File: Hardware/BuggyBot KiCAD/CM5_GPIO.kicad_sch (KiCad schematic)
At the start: 25 parts, among them J14 JST_SHBM04B-SRSS-TB, J2 Conn_02x07_Odd_Even, J3 Conn_01x03, J8 THD-20-R, J9 THD-02-R, SW1 Right angle Tact button, U1 TPD4EUSB30, U2 TPD4EUSB30, U3 MagJack-A70-112-331N126

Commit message: Removed all unnecessary components and modified PCB
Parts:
- removed J3: Conn_01x03, Connector_PinHeader_2.54mm:PinHeader_1x03_P2.54mm_Vertical, symbol Connector_Generic:Conn_01x03
- removed J9: THD-02-R, Connector_PinHeader_2.54mm:PinHeader_2x02_P2.54mm_Vertical, symbol Connector_Generic:Conn_02x02_Odd_Even
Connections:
- net BT_nDis: no longer names the net of Module1.91 (BT_nDisable)
- net SD_CLK: no longer names the net of Module1.57 (SD_CLK)
- net SD_CMD: no longer names the net of Module1.62 (SD_CMD)
- net SD_DAT0: no longer names the net of Module1.63 (SD_DAT0)
- net SD_DAT1: no longer names the net of Module1.67 (SD_DAT1)
- net SD_DAT2: no longer names the net of Module1.69 (SD_DAT2)
- net SD_DAT3: no longer names the net of Module1.61 (SD_DAT3)
- net SD_PWR_ON: no longer names the net of Module1.75 (SD_PWR_ON)
- net TR0_TAP: no longer names the net of U3.11 (VC1)
- net TR1_TAP: no longer names the net of U3.12 (VC2)
- net TR2_TAP: no longer names the net of U3.13 (VC3)
- net TR3_TAP: no longer names the net of U3.14 (VC4)
- net WL_nDis: no longer names the net of Module1.89 (WiFi_nDisable)
- no-connect marks 6 -> 19
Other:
- note added: "Activity LED (KEEP)"
- note added: "J3 removed and No-connect flags added. 10/12/26"
- note added: "POE Header removed and No-connect flags added to ethernet 10/12/26"
- note added: "PWR LED (KEEP)"
- note removed: "Activity LED"
- note removed: "Not Fitted header"
- note removed: "POE Header"
- note removed: "PWR LED"

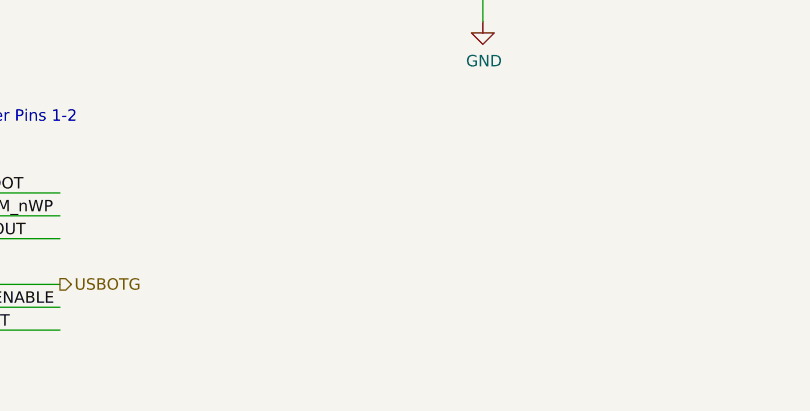
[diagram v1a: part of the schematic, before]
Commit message: Added quick connect port for IMU
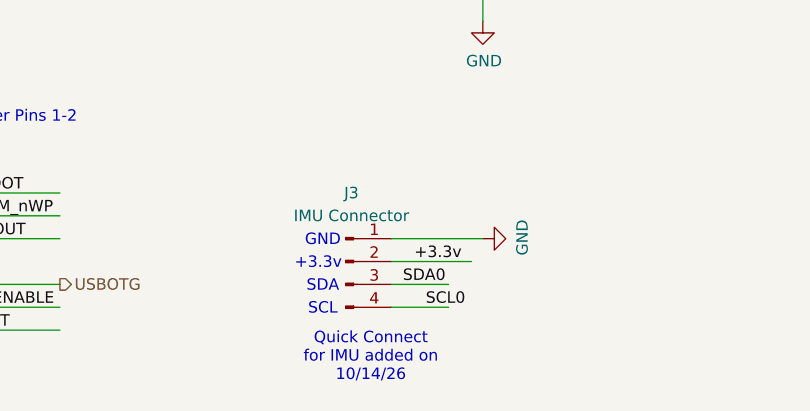
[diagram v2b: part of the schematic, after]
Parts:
- added J3: IMU Connector, Connector_JST:JST_SH_SM04B-SRSS-TB_1x04-1MP_P1.00mm_Horizontal, symbol Connector:Conn_01x04_Pin
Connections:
- net +3.3v: now also J3.2 (Pin_2)
- net GND: now also J3.1 (Pin_1)
- net SCL0: now also J3.4 (Pin_4)
- net SDA0: now also J3.3 (Pin_3)
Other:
- note added: "+3.3v"
- note added: "GND"
- note added: "Quick Connect for IMU added on 10/14/26"
- note added: "SCL"
- note added: "SDA"

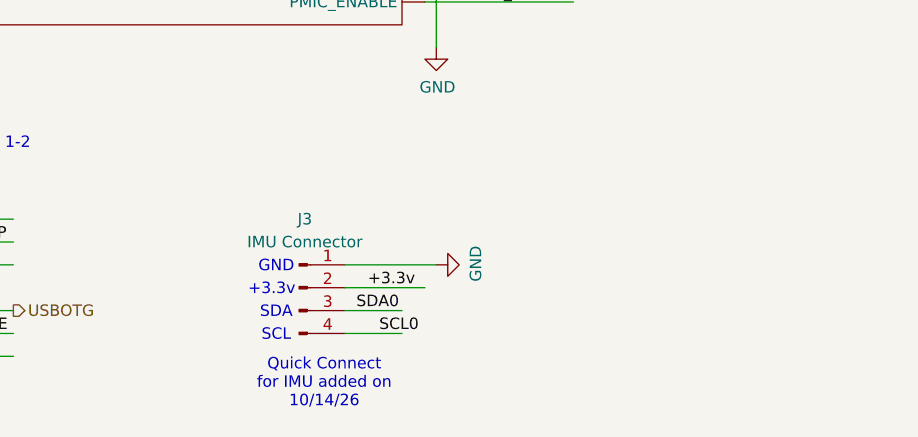
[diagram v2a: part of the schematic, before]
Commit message: Added connection port for LCD
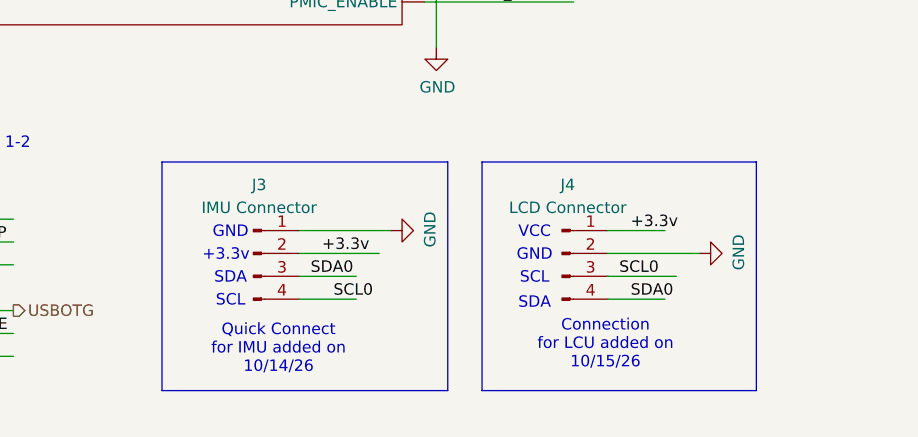
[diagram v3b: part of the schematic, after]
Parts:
- added J4: LCD Connector, Connector_JST:JST_PH_S4B-PH-K_1x04_P2.00mm_Horizontal, symbol Connector:Conn_01x04_Pin
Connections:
- net +3.3v: now also J4.1 (Pin_1)
- net GND: now also J4.2 (Pin_2)
- net SCL0: now also J4.3 (Pin_3)
- net SDA0: now also J4.4 (Pin_4)
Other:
- note added: "Connection for LCU added on 10/15/26"
- note added: "VCC"
- moved on the sheet: J3

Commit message: Updated KiCad files
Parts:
- J4: footprint Connector_JST:JST_PH_S4B-PH-K_1x04_P2.00mm_Horizontal -> Connector_JST:JST_SH_SM04B-SRSS-TB_1x04-1MP_P1.00mm_Horizontal
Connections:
- net +3.3v: now also J4.2 (Pin_2); no longer J4.1 (Pin_1)
- net GND: now also J4.1 (Pin_1); no longer J4.2 (Pin_2)
- net SCL0: now also J4.4 (Pin_4); no longer J4.3 (Pin_3)
- net SDA0: now also J4.3 (Pin_3); no longer J4.4 (Pin_4)
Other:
- note added: "Connection for LCU modified on 10/22/26"
- note removed: "Connection for LCU added on 10/15/26"
- note removed: "VCC"
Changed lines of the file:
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@@
 		)
 	)
+	(text "+3.3v"
+		(exclude_from_sim no)
+		(at 112.522 175.514 0)
+		(effects
+			(font
+				(size 1.27 1.27)
+			)
+		)
+	)
 	(text "GND"
 		(exclude_from_sim no)
@@
 		)
 	)
-	(text "GND"
+	(text "SDA"
 		(exclude_from_sim no)
-		(at 112.522 174.244 0)
+		(at 113.03 178.054 0)
 		(effects
 			(font
@@
 		)
 	)
-	(text "SCL"
-		(exclude_from_sim no)
-		(at 112.522 176.784 0)
-		(effects
-			(font
-				(size 1.27 1.27)
-			)
-		)
-	)
 	(text "FAN connector\n"
 		(exclude_from_sim no)
@@
 		)
 	)
+	(text "GND"
+		(exclude_from_sim no)
+		(at 113.03 172.974 0)
+		(effects
+			(font
+				(size 1.27 1.27)
+			)
+		)
+	)
 	(text "SDA"
 		(exclude_from_sim no)
@@
 		)
 	)
-	(text "Connection \nfor LCU added on \n10/15/26"
-		(exclude_from_sim no)
-		(at 120.396 184.15 0)
-		(effects
-			(font
-				(size 1.27 1.27)
-			)
-		)
-	)
-	(text "VCC"
+	(text "Connection \nfor LCU modified on \n10/22/26"
 		(exclude_from_sim no)
-		(at 112.522 171.704 0)
+		(at 118.872 185.166 0)
 		(effects
 			(font
@@
 		)
 	)
-	(text "SDA"
-		(exclude_from_sim no)
-		(at 112.522 179.578 0)
-		(effects
-			(font
-				(size 1.27 1.27)
-			)
-		)
-	)
 	(junction
 		(at 101.6 36.83)
@@
 	(wire
 		(pts
-			(xy 120.65 179.07) (xy 127 179.07)
+			(xy 24.13 80.01) (xy 39.37 80.01)
 		)
 		(stroke
 			(width 0)
-			(type default)
+			(type solid)
 		)
 	)
 	(wire
 		(pts
-			(xy 24.13 80.01) (xy 39.37 80.01)
+			(xy 120.65 175.26) (xy 129.54 175.26)
 		)
 		(stroke
 			(width 0)
-			(type solid)
+			(type default)
 		)
 	)
@@
 	(wire
 		(pts
-			(xy 120.65 171.45) (xy 127 171.45)
-		)
-		(stroke
-			(width 0)
-			(type default)
-		)
-	)
-	(wire
-		(pts
 			(xy 100.33 57.15) (xy 114.3 57.15)
 		)
@@
 	(wire
 		(pts
-			(xy 120.65 173.99) (xy 130.81 173.99)
-		)
-		(stroke
-			(width 0)
-			(type default)
-		)
-	)
-	(wire
-		(pts
 			(xy 100.33 69.85) (xy 114.3 69.85)
 		)
@@
 	(wire
 		(pts
+			(xy 120.65 180.34) (xy 127 180.34)
+		)
+		(stroke
+			(width 0)
+			(type default)
+		)
+	)
+	(wire
+		(pts
 			(xy 143.51 91.44) (xy 152.4 91.44)
 		)
@@
 	(wire
 		(pts
+			(xy 120.65 177.8) (xy 127 177.8)
+		)
+		(stroke
+			(width 0)
+			(type default)
+		)
+	)
+	(wire
+		(pts
 			(xy 200.66 107.95) (xy 196.85 107.95)
 		)
@@
 	(wire
 		(pts
-			(xy 120.65 176.53) (xy 128.27 176.53)
-		)
-		(stroke
-			(width 0)
-			(type default)
-		)
-	)
-	(wire
-		(pts
 			(xy 100.33 49.53) (xy 101.6 49.53)
 		)
@@
 	(wire
 		(pts
+			(xy 120.65 172.72) (xy 130.81 172.72)
+		)
+		(stroke
+			(width 0)
+			(type default)
+		)
+	)
+	(wire
+		(pts
 			(xy 140.97 41.91) (xy 152.4 41.91)
 		)
@@
 		)
 	)
+	(label "+3.3v"
+		(at 123.19 175.26 0)
+		(effects
+			(font
+				(size 1.27 1.27)
+			)
+			(justify left bottom)
+		)
+	)
 	(label "GPIO7"
 		(at 173.99 54.61 180)
@@
 		)
 	)
+	(label "SCL0"
+		(at 124.46 180.34 0)
+		(effects
+			(font
+				(size 1.27 1.27)
+			)
+			(justify left bottom)
+		)
+	)
 	(label "ETH_LEDY"
 		(at 103.124 39.37 0)
@@
 		)
 	)
-	(label "SCL0"
-		(at 121.92 176.53 0)
-		(effects
-			(font
-				(size 1.27 1.27)
-			)
-			(justify left bottom)
-		)
-	)
 	(label "CC1"
 		(at 27.94 138.43 0)
@@
 		)
 	)
+	(label "SDA0"
+		(at 121.92 177.8 0)
+		(effects
+			(font
+				(size 1.27 1.27)
+			)
+			(justify left bottom)
+		)
+	)
 	(label "GPIO19"
 		(at 148.59 67.31 180)
@@
 		)
 	)
-	(label "SDA0"
-		(at 123.19 179.07 0)
-		(effects
-			(font
-				(size 1.27 1.27)
-			)
-			(justify left bottom)
-		)
-	)
 	(label "nPWR_LED"
 		(at 104.14 140.97 0)
@@
 		)
 	)
-	(label "+3.3v"
-		(at 123.19 171.45 0)
-		(effects
-			(font
-				(size 1.27 1.27)
-			)
-			(justify left bottom)
-		)
-	)
 	(label "nRPIBOOT"
 		(at 50.546 170.18 180)
@@
 	(symbol
 		(lib_id "Connector:Conn_01x04_Pin")
-		(at 115.57 173.99 0)
+		(at 115.57 175.26 0)
 		(unit 1)
 		(body_style 1)
@@
 		(fields_autoplaced yes)
 		(property "Reference" "J4"
-			(at 116.205 166.37 0)
+			(at 116.205 167.64 0)
 			(show_name no)
 			(do_not_autoplace no)
@@
 		)
 		(property "Value" "LCD Connector"
-			(at 116.205 168.91 0)
+			(at 116.205 170.18 0)
 			(show_name no)
 			(do_not_autoplace no)
@@
 			)
 		)
-		(property "Footprint" "Connector_JST:JST_PH_S4B-PH-K_1x04_P2.00mm_Horizontal"
-			(at 115.57 173.99 0)
+		(property "Footprint" "Connector_JST:JST_SH_SM04B-SRSS-TB_1x04-1MP_P1.00mm_Horizontal"
+			(at 115.57 175.26 0)
 			(hide yes)
 			(show_name no)
@@
 		)
 		(property "Datasheet" ""
-			(at 115.57 173.99 0)
+			(at 115.57 175.26 0)
 			(hide yes)
 			(show_name no)
@@
 		)
 		(property "Description" "Generic connector, single row, 01x04, script generated"
-			(at 115.57 173.99 0)
+			(at 115.57 175.26 0)
 			(hide yes)
 			(show_name no)
@@
 			)
 		)
-		(pin "3"
-		)
-		(pin "1"
+		(pin "2"
 		)
 		(pin "4"
 		)
-		(pin "2"
+		(pin "3"
+		)
+		(pin "1"
 		)
 		(instances
@@
 	(symbol
 		(lib_id "power:GND")
-		(at 130.81 173.99 90)
+		(at 254 153.67 0)
 		(unit 1)
 		(body_style 1)
@@
 		(in_pos_files yes)
 		(dnp no)
-		(property "Reference" "#PWR033"
-			(at 137.16 173.99 0)
+		(property "Reference" "#PWR030"
+			(at 254 160.02 0)
 			(hide yes)
 			(show_name no)
@@
 		)
 		(property "Value" "GND"
-			(at 135.2042 173.863 0)
+			(at 254.127 158.0642 0)
 			(show_name no)
 			(do_not_autoplace no)
@@
 		)
 		(property "Footprint" ""
-			(at 130.81 173.99 0)
+			(at 254 153.67 0)
 			(hide yes)
 			(show_name no)
@@
 		)
 		(property "Datasheet" ""
-			(at 130.81 173.99 0)
+			(at 254 153.67 0)
 			(hide yes)
 			(show_name no)
@@
 		)
 		(property "Description" "Power symbol creates a global label with name \"GND\" , ground"
-			(at 130.81 173.99 0)
+			(at 254 153.67 0)
 			(hide yes)
 			(show_name no)
@@
 			(project "CM5IO"
 				(path "/e63e39d7-6ac0-4ffd-8aa3-1841a4541b55/00000000-0000-0000-0000-00005cff706a"
-					(reference "#PWR033")
+					(reference "#PWR030")
 					(unit 1)
 				)
@@
 	(symbol
 		(lib_id "power:GND")
-		(at 254 153.67 0)
+		(at 130.81 172.72 90)
 		(unit 1)
 		(body_style 1)
@@
 		(in_pos_files yes)
 		(dnp no)
-		(property "Reference" "#PWR030"
-			(at 254 160.02 0)
+		(property "Reference" "#PWR033"
+			(at 137.16 172.72 0)
 			(hide yes)
 			(show_name no)
@@
 		)
 		(property "Value" "GND"
-			(at 254.127 158.0642 0)
+			(at 135.2042 172.593 0)
 			(show_name no)
 			(do_not_autoplace no)
@@
 		)
 		(property "Footprint" ""
-			(at 254 153.67 0)
+			(at 130.81 172.72 0)
 			(hide yes)
 			(show_name no)
@@
 		)
 		(property "Datasheet" ""
-			(at 254 153.67 0)
+			(at 130.81 172.72 0)
 			(hide yes)
 			(show_name no)
@@
 		)
 		(property "Description" "Power symbol creates a global label with name \"GND\" , ground"
-			(at 254 153.67 0)
+			(at 130.81 172.72 0)
 			(hide yes)
 			(show_name no)
@@
 			(project "CM5IO"
 				(path "/e63e39d7-6ac0-4ffd-8aa3-1841a4541b55/00000000-0000-0000-0000-00005cff706a"
-					(reference "#PWR030")
+					(reference "#PWR033")
 					(unit 1)
 				)

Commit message: Updated KiCad files and added redesign pcb file
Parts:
- added J6, J7: Line Sensor, Connector_JST:JST_SH_SM04B-SRSS-TB_1x04-1MP_P1.00mm_Horizontal, symbol Connector:Conn_01x04_Pin
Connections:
- net +3.3v: now also J6.1 (Pin_1), J7.1 (Pin_1)
- net GND: now also J6.2 (Pin_2), J7.2 (Pin_2)
- net GPIO20: now also J6.3 (Pin_3)
- net GPIO21: now also J7.3 (Pin_3)
- no-connect marks 19 -> 21
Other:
- note added: "A0"
- note added: "D0"
- note added: "Quick Connect for Line Sensor added on 10/23/26"

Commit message: Updated KiCad files
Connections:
- net GPIO2: now also J3.3 (Pin_3), J4.3 (Pin_3)
- net GPIO3: now also J3.4 (Pin_4), J4.4 (Pin_4)
- net SCL0: no longer J3.4 (Pin_4), J4.4 (Pin_4)
- net SDA0: no longer J3.3 (Pin_3), J4.3 (Pin_3)
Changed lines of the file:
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@@
+		)
+	)
+	(label "GPIO2"
+		(at 121.92 177.8 0)
+		(effects
+			(font
+				(size 1.27 1.27)
+			)
+			(justify left bottom)
 		)
 	)
@@
 		)
 	)
-	(label "SCL0"
-		(at 124.46 180.34 0)
-		(effects
-			(font
-				(size 1.27 1.27)
-			)
-			(justify left bottom)
-		)
-	)
 	(label "ETH_LEDY"
 		(at 103.124 39.37 0)
@@
 		)
 	)
-	(label "SDA0"
-		(at 87.63 176.53 0)
-		(effects
-			(font
-				(size 1.27 1.27)
-			)
-			(justify left bottom)
-		)
-	)
 	(label "PWM"
 		(at 102.87 44.45 0)
@@
 		)
 	)
-	(label "SDA0"
-		(at 121.92 177.8 0)
-		(effects
-			(font
-				(size 1.27 1.27)
-			)
-			(justify left bottom)
-		)
-	)
 	(label "GPIO19"
 		(at 148.59 67.31 180)
@@
 		)
 	)
+	(label "GPIO3"
+		(at 121.92 180.34 0)
+		(effects
+			(font
+				(size 1.27 1.27)
+			)
+			(justify left bottom)
+		)
+	)
 	(label "GPIO20"
 		(at 175.26 69.85 180)
@@
 		)
 	)
+	(label "GPIO3"
+		(at 87.63 179.07 0)
+		(effects
+			(font
+				(size 1.27 1.27)
+			)
+			(justify left bottom)
+		)
+	)
 	(label "TRD0_N"
 		(at 245.11 26.67 180)
@@
 		)
 	)
-	(label "SCL0"
-		(at 90.17 179.07 0)
-		(effects
-			(font
-				(size 1.27 1.27)
-			)
-			(justify left bottom)
-		)
-	)
 	(label "GPIO23"
 		(at 175.26 41.91 180)
@@
 		)
 	)
+	(label "GPIO2"
+		(at 88.9 176.53 0)
+		(effects
+			(font
+				(size 1.27 1.27)
+			)
+			(justify left bottom)
+		)
+	)
